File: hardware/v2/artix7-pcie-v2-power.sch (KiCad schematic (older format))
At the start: 40 parts

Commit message: v2 power schematic : annotated
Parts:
- added C10, C7: 22uF/10V/X5R, tom-passives:C_0603_1608Metric_Pad1.05x0.95mm_HandSolder, symbol tom-passives:C
- added C18, C21: 1uF/6.3V/X5R, tom-passives:C_0402_1005Metric, symbol tom-passives:C
- added R20: 0R, tom-passives:C_0402_1005Metric, symbol tom-passives:R
- added U7: LP5907MFX, tom-semiconductors:SOT-23-5, symbol tom-semiconductors:LP5907MFX
- C11, C19, C20, C9: renamed from C?; footprint (none) -> tom-passives:C_0402_1005Metric
- C12, C13, C14, C15, C16, C17, C2, C3, C4, C5, C6, C8: renamed from C?; footprint (none) -> tom-passives:C_0603_1608Metric_Pad1.05x0.95mm_HandSolder
- gave numbers to parts that had none: 24
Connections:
- net labels added: +1V2, VIN_1.0, VIN_1.2V, VIN_1.5, VIN_1.8, VIN_3.3
- net labels removed: +1.0VOUT, +1.5VOUT, +1.8VOUT, +3.3VOUT, +5VIN, 5V_1.0, 5V_1.5, 5V_1.8, 5V_3.3
- wire segments 200 -> 198

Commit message: v2 schematic: add bank14, serdes, fpga footprint
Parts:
- renumbered C9 to C10, C10 to C11, C11 to C12, C12 to C13, C13 to C14, C14 to C15, C15 to C16, C16 to C17, C17 to C18, C18 to C19, C19 to C20, C20 to C21, C21 to C22, C2 to C3, C3 to C4, C4 to C5, C5 to C6, C6 to C7, C7 to C8, C8 to C9, R5 to R10, R6 to R11, R7 to R12, R8 to R13, R9 to R14, R10 to R15, R11 to R16, R12 to R17, R13 to R18, R14 to R19, R15 to R20, R16 to R21, R17 to R22, R18 to R23, R19 to R24, R20 to R25, R4 to R9

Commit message: v2 schematic: moved 1.0V regulator to APXS006A0X4-SRZ
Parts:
- removed C9: 10uF/6.3V/X5R, tom-passives:C_0603_1608Metric_Pad1.05x0.95mm_HandSolder, symbol tom-passives:C
- removed L2: 0.50uH, symbol tom-passives:INDUCTOR_SMALL
- removed R14: 402K/1%, tom-passives:C_0402_1005Metric, symbol tom-passives:R
- removed R16: 100K/1%, tom-passives:C_0402_1005Metric, symbol tom-passives:R
- removed U4: FAN53541, symbol tom-semiconductors:FAN53541
- added C?: 15nF/6.3V/X7R, tom-passives:C_0402_1005Metric, symbol tom-passives:C
- added R?: 100k/5%, tom-passives:C_0402_1005Metric, symbol tom-passives:R
- added R?: 14.45k/0.5%, tom-passives:C_0402_1005Metric, symbol tom-passives:R
- added R?: 100R/1%, tom-passives:C_0402_1005Metric, symbol tom-passives:R
- added X?: APXS006A0X4-SRZ, symbol tom-modules:APXS006A0X4-SRZ
- C4: value 10uF/6.3V/X5R -> 10uF/25V/X5R
- C6: value 10uF/6.3V/X7R -> 10uF/25V/X7R
- R10, R17, R18, R9: footprint tom-passives:C_0402_1005Metric -> tom-passives:C_0603_1608Metric
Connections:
- net labels removed: FB_1.0V
- wire segments 198 -> 171
- no-connect marks 0 -> 1
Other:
- moved on the sheet: C4, C6, R10

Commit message: sch: moved all power supplies to APXS006A0X4-SRZ
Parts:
- removed C10, C20, C21: 10nF/6.3V/X7R, tom-passives:C_0402_1005Metric, symbol tom-passives:C
- removed C13, C14, C17, C18, C3, C7: 10uF/6.3V/X5R, tom-passives:C_0603_1608Metric_Pad1.05x0.95mm_HandSolder, symbol tom-passives:C
- removed C15, C16, C5: 10uF/6.3V/X7R, tom-passives:C_0603_1608Metric_Pad1.05x0.95mm_HandSolder, symbol tom-passives:C
- removed L1, L3, L4: 0.56uH, symbol tom-passives:INDUCTOR_SMALL
- removed R11, R19, R21: 100k/5%, tom-passives:C_0402_1005Metric, symbol tom-passives:R
- removed R12: 115K/1%, tom-passives:C_0402_1005Metric, symbol tom-passives:R
- removed R15, R23, R24: 100K/1%, tom-passives:C_0402_1005Metric, symbol tom-passives:R
- removed R17, R18, R9: 0R, tom-passives:C_0603_1608Metric, symbol tom-passives:R
- removed R20: 31.6K/1%, tom-passives:C_0402_1005Metric, symbol tom-passives:R
- removed R22: 80.6K/1%, tom-passives:C_0402_1005Metric, symbol tom-passives:R
- removed U3, U5, U6: FAN53541, symbol tom-semiconductors:FAN53541
- added C? (x2): 10uF/25V/X7R, tom-passives:C_0603_1608Metric_Pad1.05x0.95mm_HandSolder, symbol tom-passives:C
- added C? (x2): 10uF/25V/X5R, tom-passives:C_0603_1608Metric_Pad1.05x0.95mm_HandSolder, symbol tom-passives:C
- added C? (x2): 15nF/6.3V/X7R, tom-passives:C_0402_1005Metric, symbol tom-passives:C
- added C? (x2): 100uF/6.3V/TANT, tom-passives:C_0402_1005Metric, symbol tom-passives:C
- added R?: 18k/0.5%, tom-passives:C_0402_1005Metric, symbol tom-passives:R
- added R? (x2): 0R, tom-passives:C_0603_1608Metric, symbol tom-passives:R
- added R? (x2): 100k/5%, tom-passives:C_0402_1005Metric, symbol tom-passives:R
- added R?: 19.8k/0.5%, tom-passives:C_0402_1005Metric, symbol tom-passives:R
- added R? (x2): 100R/1%, tom-passives:C_0402_1005Metric, symbol tom-passives:R
- added R?: 6.49k/0.5%, tom-passives:C_0402_1005Metric, symbol tom-passives:R
- added R?: 24.0k/0.5%, tom-passives:C_0402_1005Metric, symbol tom-passives:R
- added R?: 2.40k/0.5%, tom-passives:C_0402_1005Metric, symbol tom-passives:R
- added X? (x2): APXS006A0X4-SRZ, symbol tom-modules:APXS006A0X4-SRZ
- C11, C8: value 22uF/10V/X5R -> 22uF/25V/X5R
- C12: value 10nF/6.3V/X7R -> 100uF/6.3V/TANT; Digikey (none) -> 478-9393-1-ND
- R?: value 14.45k/0.5% -> 73.2k/0.5%
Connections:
- net labels added: +3V3, TRIM_1.0V, TRIM_1.8V, TRIM_3.3V, VCC, VCC_1.0, VCC_1.8, VCC_3.3
- net labels removed: +1V5, +5V, FB_1.5V, FB_1.8V, FB_3.3V, PGOOD_1.5V, VIN_1.0, VIN_1.5, VIN_1.8, VIN_3.3
- wire segments 171 -> 66
- no-connect marks 1 -> 3
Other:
- note added: "19.8k//6.49k=4.8878k (want 4.888k)"
- note added: "24k//2.4k=2.1818 (want 2.182k)"
- note added: "73.2k//18.0k=14.447k (want 14.45k)"
- note added: "Sequence #2 1.8V\nVCCAUX"
- note added: "Sequence #3 1.2V\nVTT"
- note removed: "Sequence #2 1.8V\nVCCINT/VCCBRAM"
- note removed: "Sequence #3 1.5V\nVCCO"
- moved on the sheet: C11, C12, C19, C22, C8, C?, R25, R?, U7

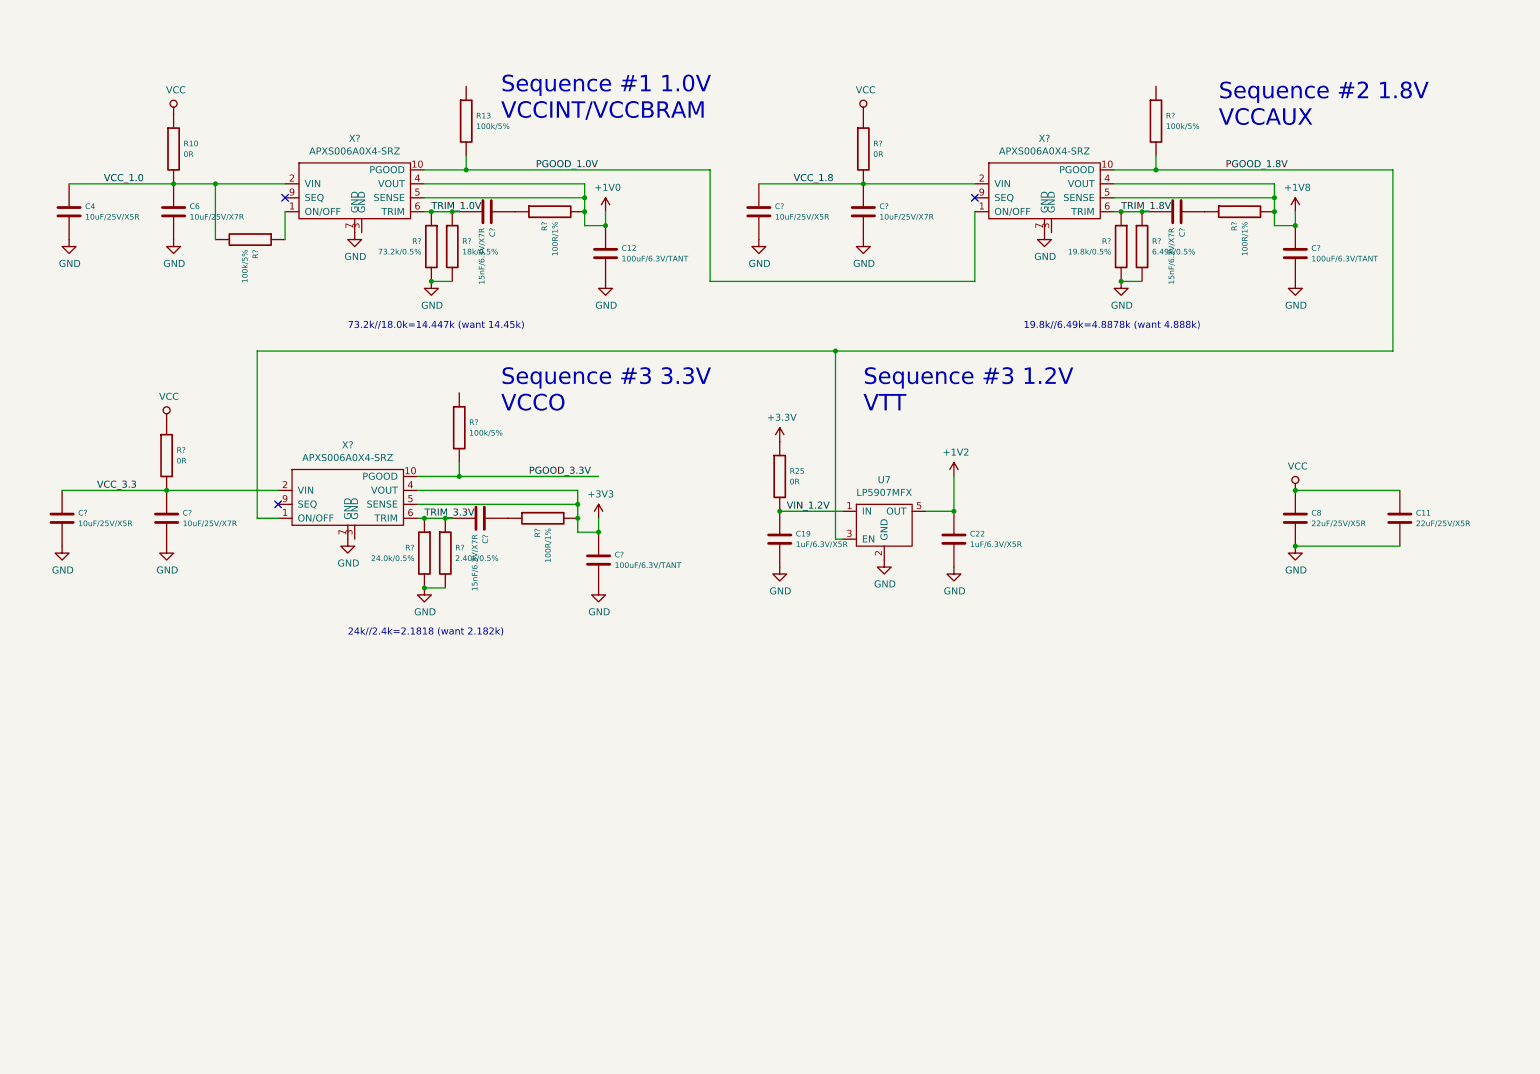
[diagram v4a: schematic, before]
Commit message: v2 hardware - all io connectors in schematic
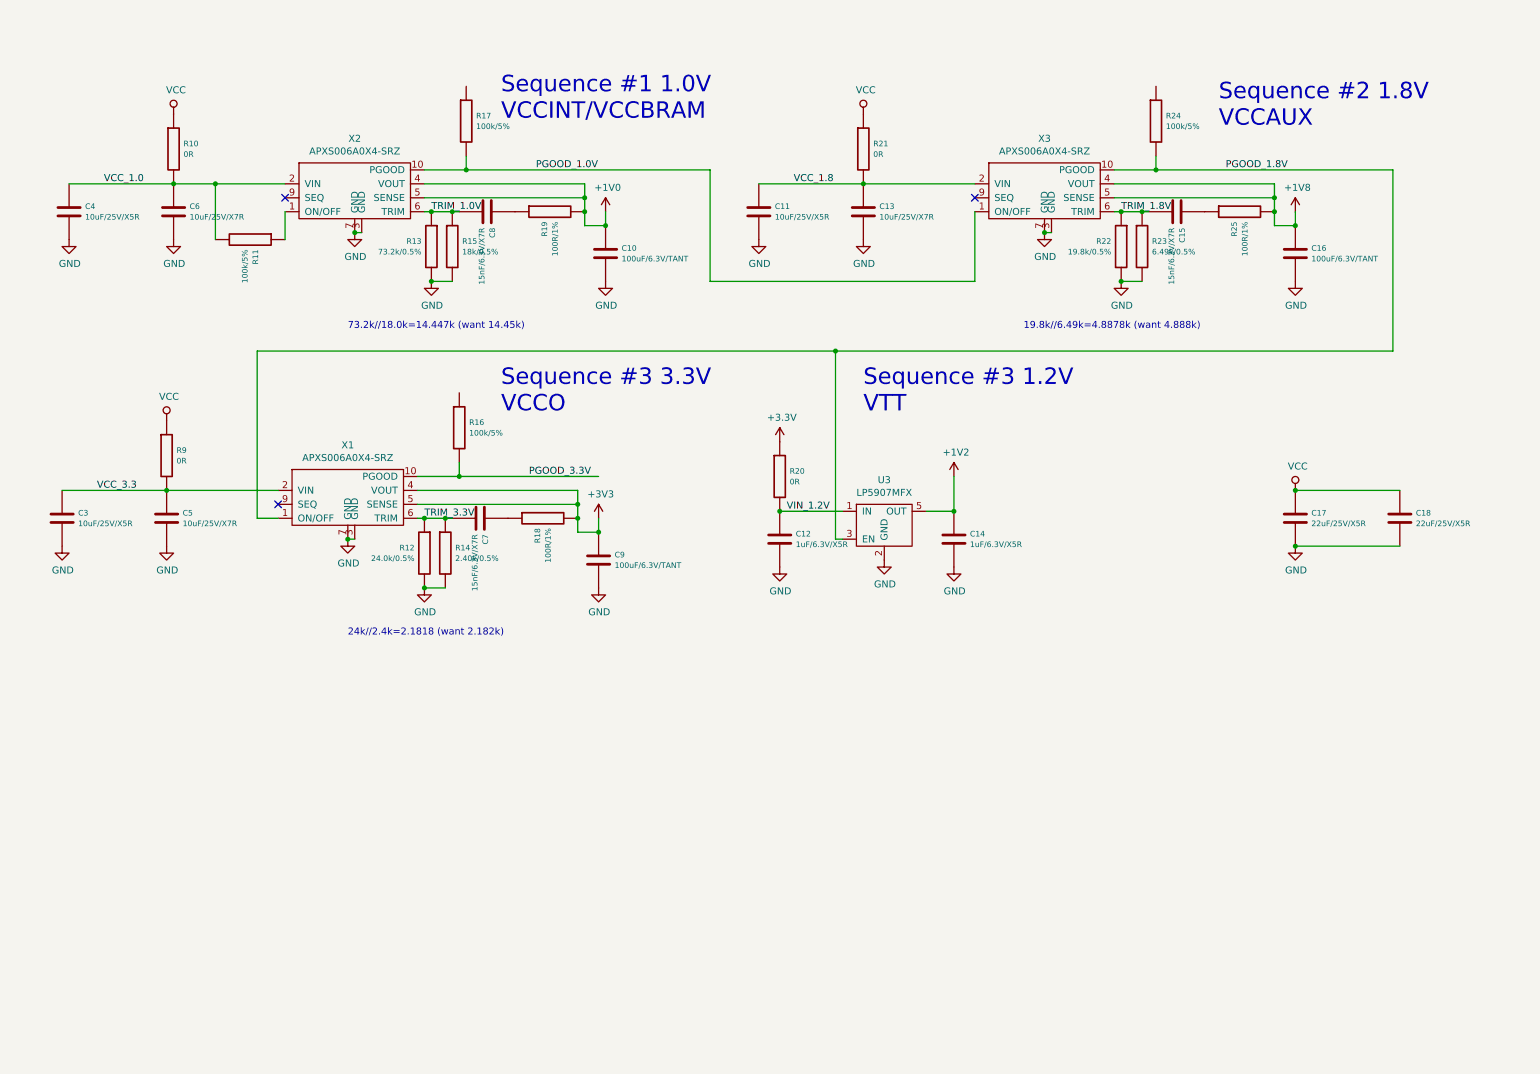
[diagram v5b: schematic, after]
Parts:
- X1, X2, X3: renamed from X?; footprint (none) -> tom-modules:APXS006
- gave numbers to parts that had none: 23
- renumbered C12 to C10, C19 to C12, C22 to C14, C8 to C17, C11 to C18, R13 to R17, R25 to R20, U7 to U3
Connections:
- net GND: now also X1.3 (GND), X2.3 (GND), X3.3 (GND)

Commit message: v2 schematic/pcb: band 13 to NC for smaller device compatibility
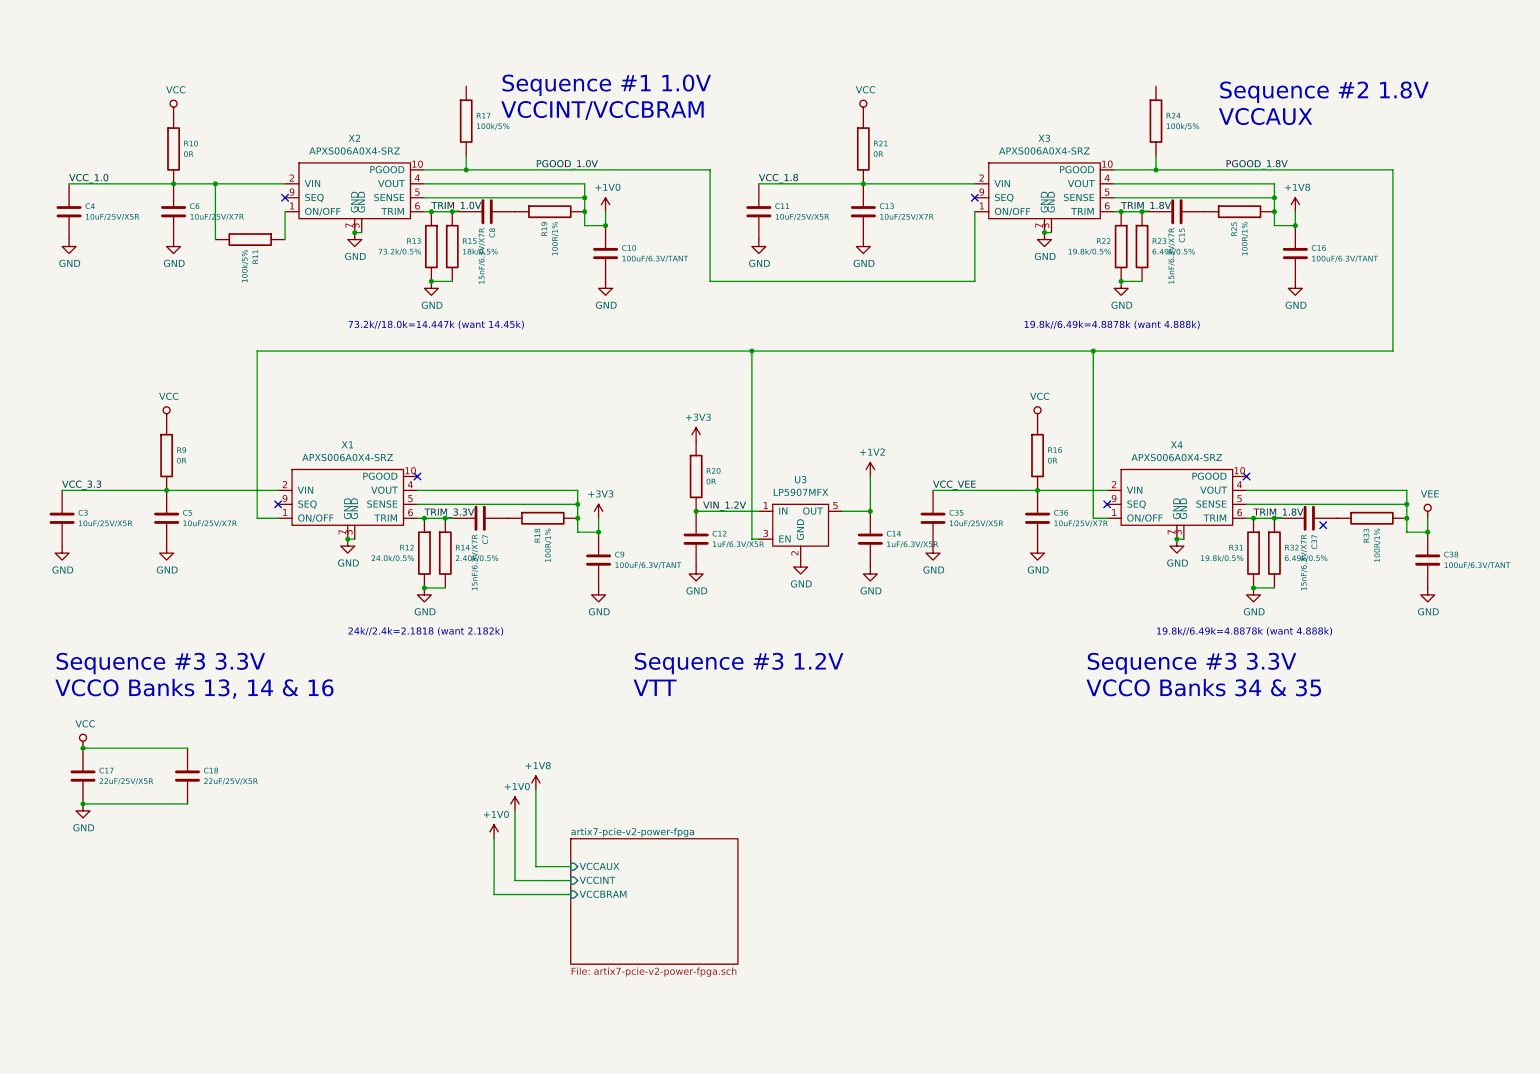
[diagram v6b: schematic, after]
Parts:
- added C35: 10uF/25V/X5R, tom-passives:C_0603_1608Metric_Pad1.05x0.95mm_HandSolder, symbol tom-passives:C
- added C36: 10uF/25V/X7R, tom-passives:C_0603_1608Metric_Pad1.05x0.95mm_HandSolder, symbol tom-passives:C
- added C37: 15nF/6.3V/X7R, tom-passives:C_0402_1005Metric, symbol tom-passives:C
- added C38: 100uF/6.3V/TANT, tom-passives:C_0402_1005Metric, symbol tom-passives:C
- added R31: 19.8k/0.5%, tom-passives:C_0402_1005Metric, symbol tom-passives:R
- added R32: 6.49k/0.5%, tom-passives:C_0402_1005Metric, symbol tom-passives:R
- added R33: 100R/1%, tom-passives:C_0402_1005Metric, symbol tom-passives:R
- added X4: APXS006A0X4-SRZ, tom-modules:APXS006, symbol tom-modules:APXS006A0X4-SRZ
- R16: value 100k/5% -> 0R; footprint tom-passives:C_0402_1005Metric -> tom-passives:C_0603_1608Metric
- R21: footprint tom-passives:C_0603_1608Metric -> tom-passives:C_0402_1005Metric
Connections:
- net GND: now also C35.2, C36.2, C38.2, R31.2, R32.2, X4.3 (GND), X4.7 (GND)
- net PGOOD_1.8V: now also X4.1 (ON/OFF)
- net TRIM_1.8V: now also C37.2, R31.1, R32.1, X4.6 (TRIM)
- net VCC: now also R16.1
- net PGOOD_3.3V: no longer names the net of X1.10 (PGOOD)
- net PGOOD_3.3V: no longer R16.2
- new net: C37.1, R33.1
- new net VCC_VEE: C35.1, C36.1, R16.2, X4.2 (VIN)
- new net VEE: C38.1, R33.2, X4.4 (VOUT), X4.5 (SENSE)
- no-connect marks 3 -> 7
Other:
- note added: "Sequence #3 3.3V\nVCCO Banks 13, 14 & 16"
- note added: "Sequence #3 3.3V\nVCCO Banks 34 & 35"
- note removed: "Sequence #3 3.3V\nVCCO"
- moved on the sheet: C12, C14, C17, C18, R20, U3

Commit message: v2 hardware progress checkin, just prior to replacing p/s with TI parts
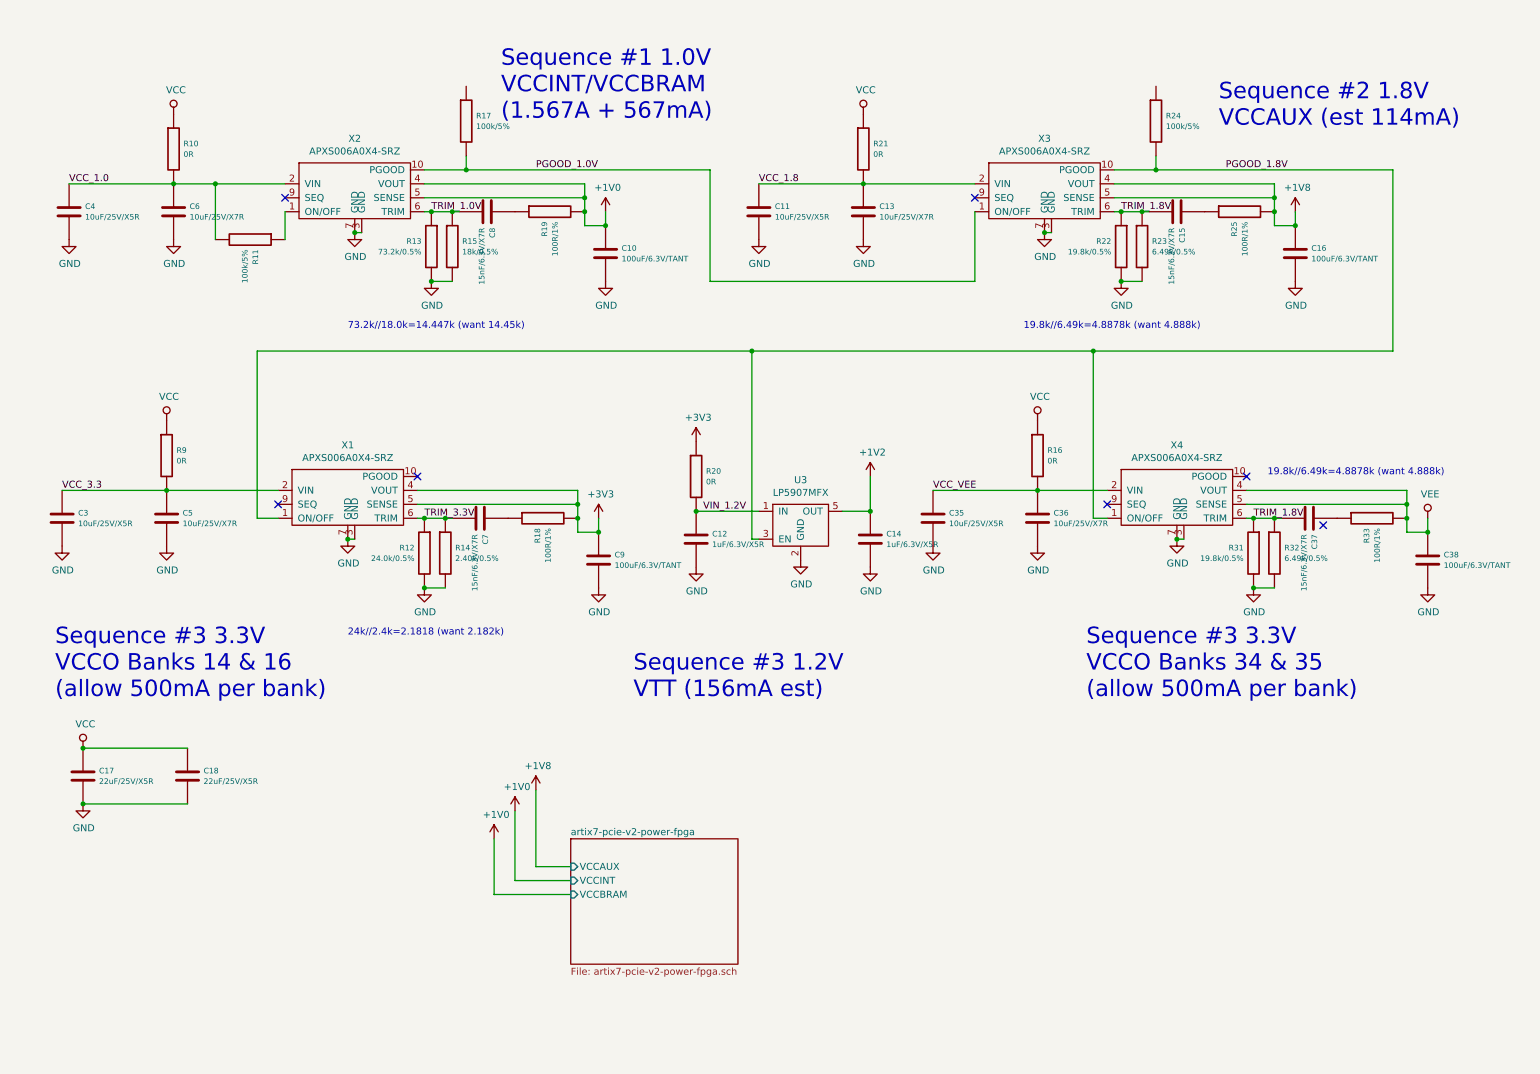
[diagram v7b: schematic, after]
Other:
- note added: "Sequence #1 1.0V\nVCCINT/VCCBRAM\n(1.567A + 567mA)"
- note added: "Sequence #2 1.8V\nVCCAUX (est 114mA)"
- note added: "Sequence #3 1.2V\nVTT (156mA est)"
- note added: "Sequence #3 3.3V\nVCCO Banks 14 & 16\n(allow 500mA per bank)"
- note added: "Sequence #3 3.3V\nVCCO Banks 34 & 35\n(allow 500mA per bank)"
- note removed: "Sequence #1 1.0V\nVCCINT/VCCBRAM"
- note removed: "Sequence #2 1.8V\nVCCAUX"
- note removed: "Sequence #3 1.2V\nVTT"
- note removed: "Sequence #3 3.3V\nVCCO Banks 13, 14 & 16"
- note removed: "Sequence #3 3.3V\nVCCO Banks 34 & 35"
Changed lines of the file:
@@
 PGOOD_1.0V
 Text Notes 700  5050 0    118  ~ 0
-Sequence #3 3.3V\nVCCO Banks 13, 14 & 16
+Sequence #3 3.3V\nVCCO Banks 14 & 16\n(allow 500mA per bank)
 $Comp
 L tom-semiconductors:LP5907MFX U3
@@
 	3350 1450 4500 1450
 Text Notes 9050 950  0    118  ~ 0
-Sequence #2 1.8V\nVCCAUX
+Sequence #2 1.8V\nVCCAUX (est 114mA)
 $Comp
 L power:GND #PWR043
@@
 	4650 1550 4650 1650
 Text Notes 3900 900  0    118  ~ 0
-Sequence #1 1.0V\nVCCINT/VCCBRAM
+Sequence #1 1.0V\nVCCINT/VCCBRAM\n(1.567A + 567mA)
 Connection ~ 4650 1650
 $Comp
@@
 	8600 1250 10300 1250
 Text Notes 4850 5050 0    118  ~ 0
-Sequence #3 1.2V\nVTT
+Sequence #3 1.2V\nVTT (156mA est)
 Wire Wire Line
 	5700 2550 5700 3900
@@
 Text Label 9300 3750 0    50   ~ 0
 TRIM_1.8V
-Text Notes 8600 4600 0    50   ~ 0
+Text Notes 9400 3450 0    50   ~ 0
 19.8k//6.49k=4.8878k (want 4.888k)
 Wire Wire Line
@@
 	1    0    0    -1
 $EndComp
-Text Notes 8100 5050 0    118  ~ 0
-Sequence #3 3.3V\nVCCO Banks 34 & 35
 Text Label 7000 3550 0    50   ~ 0
 VCC_VEE
+Text Notes 8100 5050 0    118  ~ 0
+Sequence #3 3.3V\nVCCO Banks 34 & 35\n(allow 500mA per bank)
 $EndSCHEMATC
